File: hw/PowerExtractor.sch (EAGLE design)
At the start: 38 parts, among them IC1 LM358N, Q1 IRLML5203, Q2 BSS123, T1 IRL530N

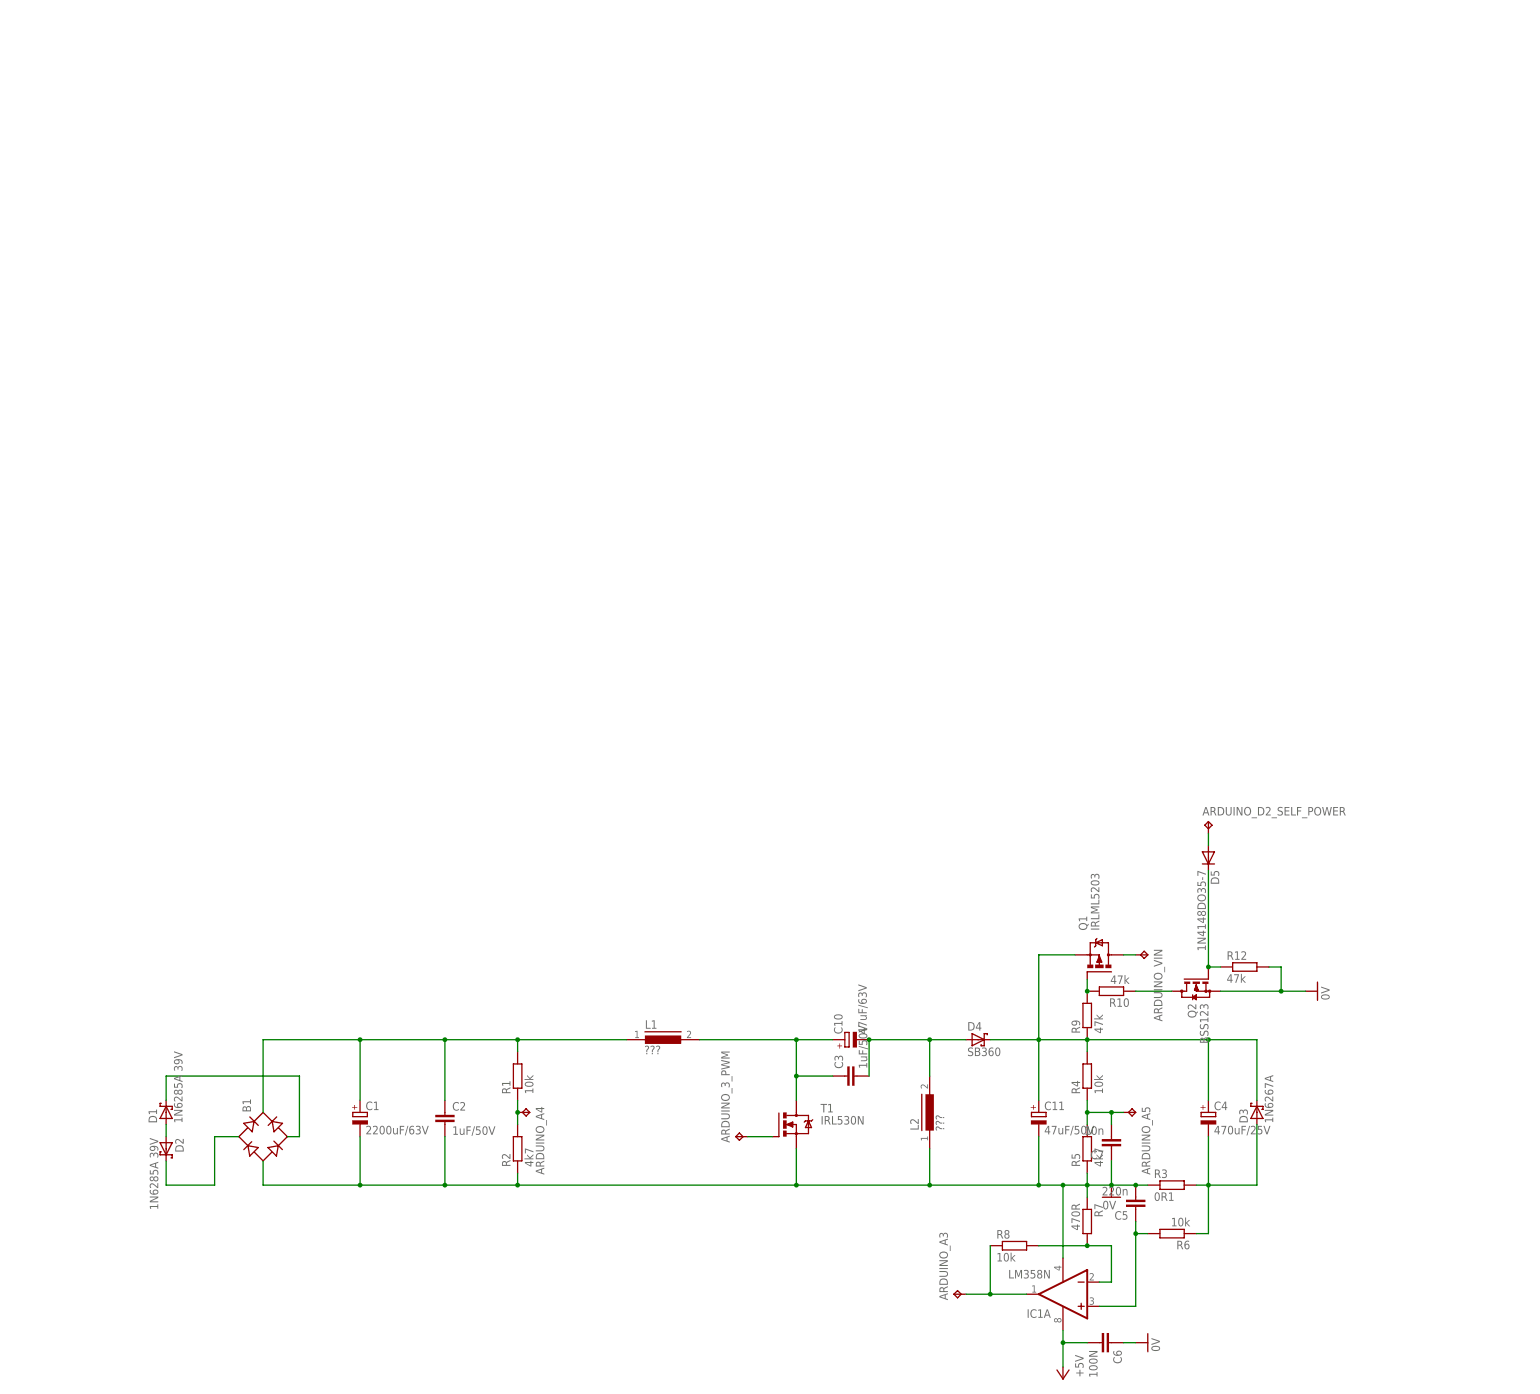
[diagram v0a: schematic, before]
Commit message: Modifications of schematic and added library with components
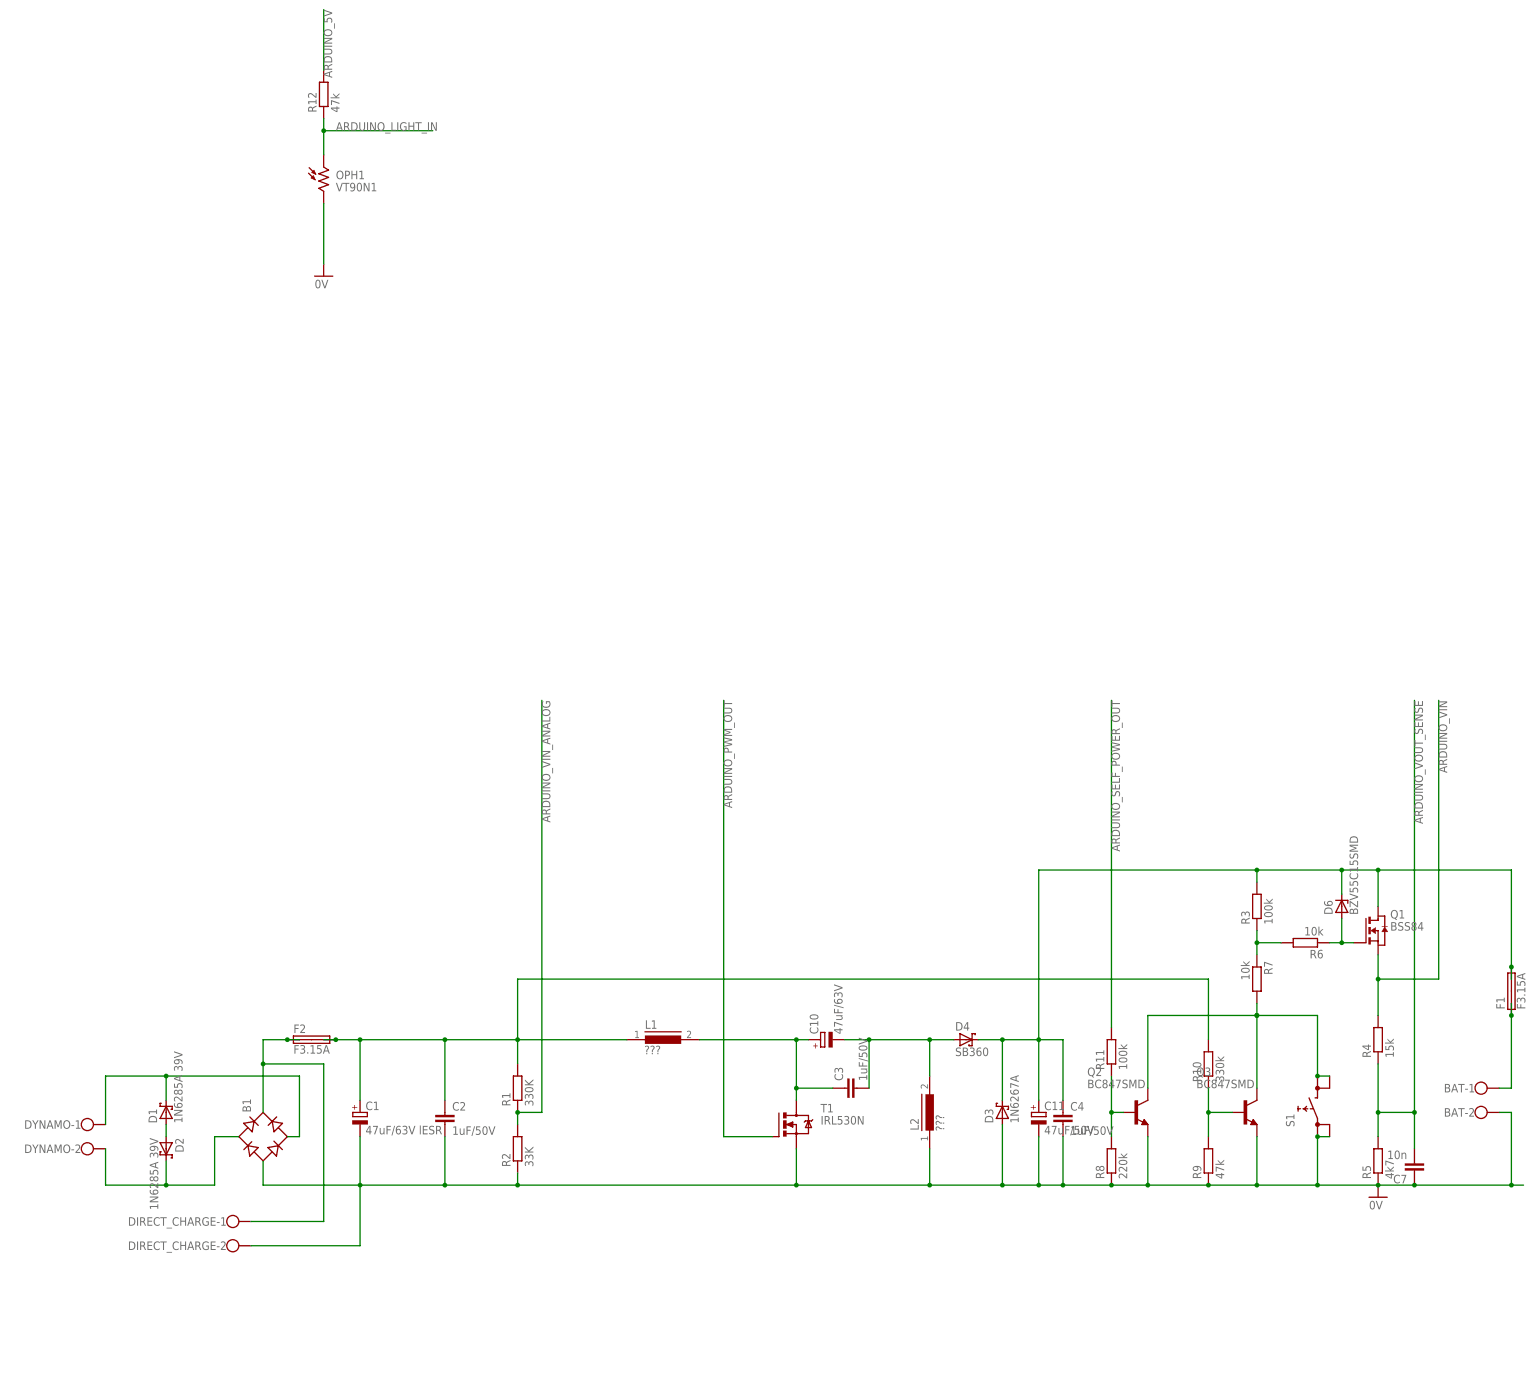
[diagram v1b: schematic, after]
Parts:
- removed ARDUINO_3_PWM, ARDUINO_A3, ARDUINO_A4, ARDUINO_A5, ARDUINO_D2_SELF_POWER, ARDUINO_VIN: TPB2,54, testpad:TPB2,54
- removed C5: 220n, rcl:C-EUC0805
- removed C6: 100N, rcl:C-EUC0805
- removed D5: 1N4148DO35-7, diode:1N4148DO35-7
- removed IC1: LM358N, linear:LM358N
- added BAT, DIRECT_CHARGE, DYNAMO: (no value), con-wago-500:W237-102
- added D6: BZV55C15SMD, diode:ZENER-DIODESOD80C
- added F1, F2: F3.15A, fuse:SHK20L
- added OPH1: VT90N1, photo-elements:VT90N1
- added Q3: BC847SMD, triakcz:BC847SMD
- added R11: 100k, rcl:R-EU_R0805
- added S1: (no value), triakcz:TL1105
- C1: value 2200uF/63V -> 47uF/63V lESR; device rcl:CPOL-EUE10-22.5 -> rcl:CPOL-EUE5-8.5
- C4: value 470uF/25V -> 1uF/50V; device rcl:CPOL-EUE5-10.5 -> rcl:C-EUC0805
- Q1: value IRLML5203 -> BSS84; device transistor-power:IRLML5203 -> triakcz:BSS84
- Q2: value BSS123 -> BC847SMD; device transistor-small-signal:BSS123 -> triakcz:BC847SMD
- R1: value 10k -> 330K
- R10: value 47k -> 330k
- R2: value 4k7 -> 33K
- R3: value 0R1 -> 100k; device rcl:R-EU_0414/15 -> rcl:R-EU_R0805
- R4: value 10k -> 15k
- R7: value 470R -> 10k
- R8: value 10k -> 220k
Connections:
- removed net +5V: C6.2, IC1P.V+
- removed net ARDUINO_A3: ARDUINO_A3.TP, IC1A.OUT, R8.1
- removed net ARDUINO_A4: ARDUINO_A4.TP, R1.1, R2.2
- removed net ARDUINO_A5: ARDUINO_A5.TP, C7.2, R4.1, R5.2
- removed net N$12: Q2.D, R10.1
- removed net N$13: D5.C, Q2.G, R12.1
- removed net N$14: ARDUINO_D2_SELF_POWER.TP, D5.A
- removed net N$8: ARDUINO_VIN.TP, Q1.D
- new net ARDUINO_5V: R12.2
- new net ARDUINO_LIGHT_IN: OPH1.1, R12.1
- new net ARDUINO_PWM_OUT: T1.G
- new net ARDUINO_SELF_POWER_OUT: R11.2
- new net ARDUINO_VIN: Q1.S, R4.2
- new net ARDUINO_VIN_ANALOG: R1.1, R2.2
- new net ARDUINO_VOUT_SENSE: C7.2, R4.1, R5.2
- new net GND: B1.-, BAT-2.KL, C1.-, C11.-, C2.2, C4.2, C7.1, D3.A, DIRECT_CHARGE-2.KL, L2.1, Q2.E, Q3.E, R2.1, R5.1, R8.1, R9.1, S1.0@A, S1.0@B, T1.S
- new net N$15: Q2.B, R11.1, R8.2
- new net VIN: C1.+, C2.1, F2.2A, F2.2B, L1.1, R1.2, R10.2
- net 0V: now also OPH1.2; no longer B1.-, C1.-, C11.-, C2.2, C5.2, C6.1, C7.1, IC1P.V-, L2.1, Q2.S, R12.2, R2.1, R3.1, R5.1, R7.1, T1.S
- net HUB2: now also DYNAMO-2.KL
- net HUB_1: now also DYNAMO-1.KL
- net N$10: now also B1.+, DIRECT_CHARGE-1.KL, F2.1A, F2.1B; no longer Q1.G, R10.2, R9.2
- net N$11: now also BAT-1.KL, F1.1A, F1.1B; no longer IC1A.-IN, R7.2, R8.2
- net N$4: now also Q3.B, R10.1, R9.2; no longer C11.+, C4.+, D3.C, D4.C, Q1.S, R4.2, R9.1
- net N$5: now also C11.+, C4.1, D3.C, D4.C, D6.C, F1.2A, F1.2B, Q1.D, R3.2; no longer ARDUINO_3_PWM.TP, T1.G
- net N$6: now also Q2.C, Q3.C, R7.2, S1.1@A, S1.1@B; no longer B1.+, C1.+, C2.1, L1.1, R1.2
- net N$7: now also D6.A, Q1.G; no longer C4.-, D3.A, R3.2
- net N$9: now also R3.1, R7.1; no longer C5.1, IC1A.+IN
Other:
- moved on the sheet: C10, C3, C7, D3, D4, R1, R10, R12, R3, R4, R5, R6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

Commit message: Add 5V USB out, 12V out, both controlled by arduino
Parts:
- added 12VOUT, 5VOUT, HEAD_LED, TAIL_LED: (no value), con-wago-500:W237-102
- added C5: 10n, rcl:C-EUC0805
- added C6, C8: 100n, rcl:C-EUC0805
- added D5: BZV55C15SMD, diode:ZENER-DIODESOD80C
- added D7, D8: 1N4148MINIMELF, triakcz:1N4148MINIMELF
- added F3, F4: F1.5A, fuse:SHK20L
- added Q4: BC847SMD, triakcz:BC847SMD
- added R13, R14, R15: 0R01, rcl:R-EU_M1206
- added R16: 1k5, rcl:R-EU_R0805
- added R17, R18, R21, R23: 100k, rcl:R-EU_R0805
- added R19: 330k, rcl:R-EU_R0805
- added R20, R22: 2k2, rcl:R-EU_R0805
- added RECOM-785.0-1.0: (no value), v-reg:78XXS
- added T2: IRF7416, triakcz:IRF7416
- added T3, T4: IRLL014N_, triakcz:IRLL014N_
- added U$1: LDD700L, triakcz:LDD700L
- added U1: ZXCT1086E5TA, triakcz:ZXCT1086E5TA
- R7: value 10k -> 220R
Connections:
- new net +OUT: 12VOUT-2.KL, F4.2A, F4.2B, RECOM-785.0-1.0.IN
- new net ARDUINO_IOUT_SENSE: C5.2, R16.2
- new net ARDUINO_MAIN_LIGHT_CTRL: R17.2
- new net ARDUINO_OUT_CHARGE_OUTPUT_CONTROL: R22.2
- new net ARDUINO_OUT_TAIL_LIGHT: R20.2
- new net GND1: R23.2, T4.S
- new net N$12: R14.2, R15.1
- new net N$13: C11.+, C4.1, D3.C, D4.C, R13.1, U1.S+
- new net N$14: C6.1, D5.A, R19.1, R7.2, T2.G
- new net N$16: R16.1, U1.OUT
- new net N$17: Q4.B, R17.1, R18.1
- new net N$18: D7.A, R7.1
- new net N$19: C8.2, T2.D, U$1.VCC
- new net N$20: D8.A, U$1.PWM
- new net N$21: HEAD_LED-2.KL, U$1.OUT+
- new net N$22: HEAD_LED-1.KL, U$1.OUT-
- new net N$23: C6.2, D5.C, F3.2A, F3.2B, R19.2, T2.S, TAIL_LED-2.KL
- new net N$24: R20.1, R21.1, T3.G
- new net N$25: T3.D, TAIL_LED-1.KL
- new net N$26: 5VOUT-2.KL, RECOM-785.0-1.0.OUT
- new net N$27: R22.1, R23.1, T4.G
- new net N$28: 12VOUT-1.KL, 5VOUT-1.KL, RECOM-785.0-1.0.GND, T4.D
- new net N$8: R13.2, R14.1
- net ARDUINO_5V: now also U1.VCC
- net GND: now also C5.1, C8.1, Q4.E, R18.2, R21.2, T3.S, U$1.GND, U1.GND
- net N$5: now also F3.1A, F3.1B, F4.1A, F4.1B, R15.2, U1.S-; no longer C11.+, C4.1, D3.C, D4.C
- net N$6: now also R3.1, R6.2; no longer R7.2
- net N$9: now also D7.C, D8.C, Q4.C; no longer R3.1, R6.2, R7.1
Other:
- moved on the sheet: R7
